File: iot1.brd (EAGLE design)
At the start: 95 x 100 mm, 77 parts, among them IC1 MEGA8-P, IC2 7805T, IC3 LTC2486C, IC4 7805T, IC5 4051N, IC6 OPA2134PA, IC8 MAX3468CPA, J1 DCJ0202, U2 HTU21D, U3 LM2577T-ADJ/NOPB, X1 22-23-2041, X2 A1944-50, X4 22-23-2041, X5 22-23-2041

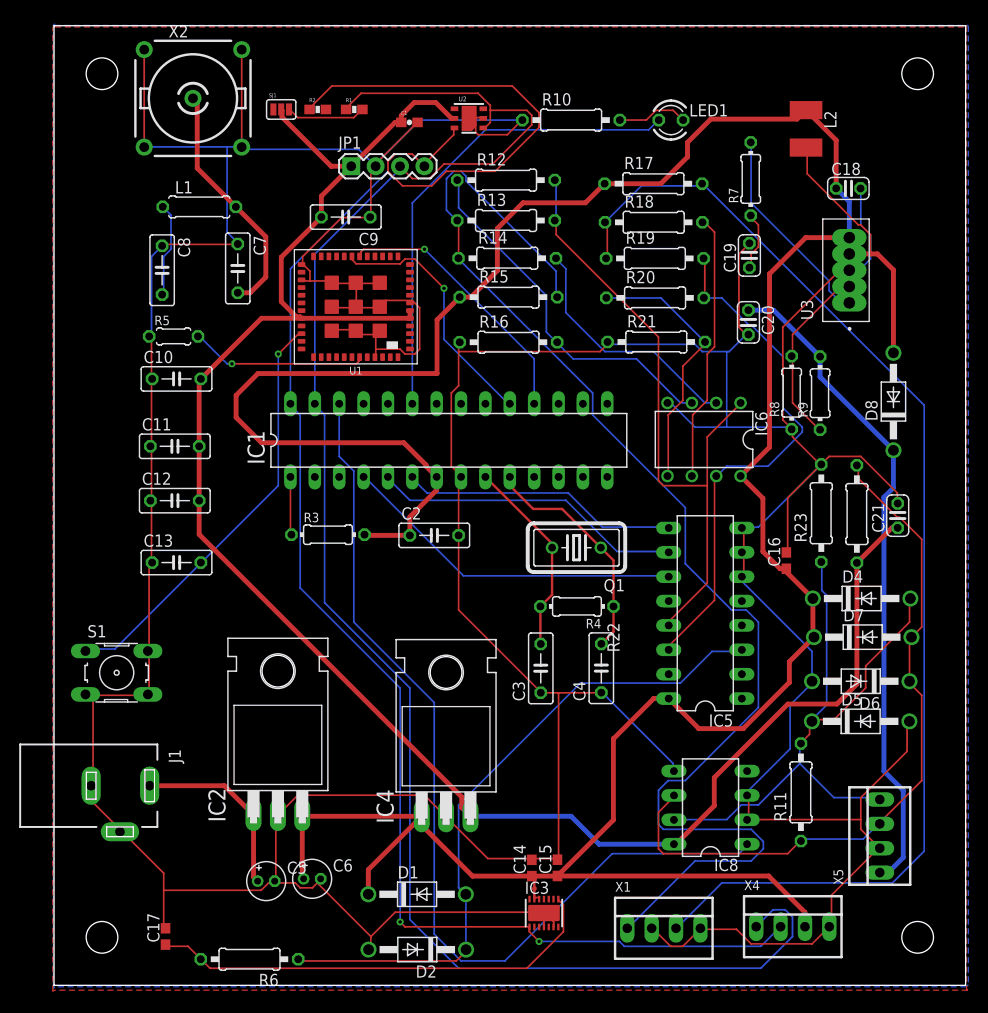
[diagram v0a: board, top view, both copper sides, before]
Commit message: renumbering board components
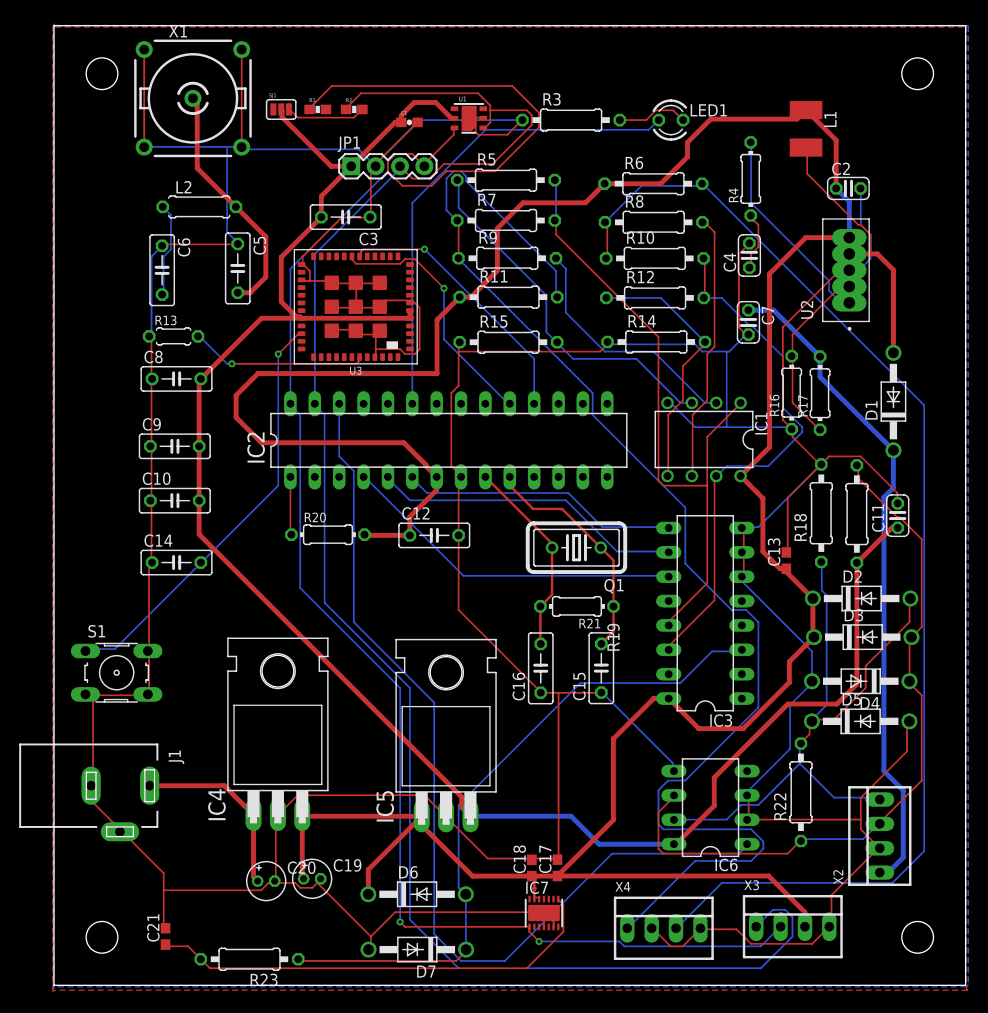
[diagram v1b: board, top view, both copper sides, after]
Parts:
- removed D8: 1N4004, diode:DO41-10
- removed IC8: MAX3468CPA, maxim:DIL08
- removed X5: 22-23-2041, con-molex:22-23-2041
- added D3: 1N4004, diode:DO41-10
- added IC7: LTC2486C, linear-technology:DFN14-4X3
- added X3: 22-23-2041, con-molex:22-23-2041
- C10: value 0.1u -> 10u
- C11: value 1u -> (none); device rcl:C050-025X075 -> rcl:C025-024X044
- C12: value 10u -> (none)
- C13: value 0.1u -> (none); device rcl:C050-025X075 -> rcl:C0603
- C14: value (none) -> 0.1u; device rcl:C0603 -> rcl:C050-025X075
- C15, C16: device rcl:C0603 -> rcl:C050-025X075
- C18: value 0.1uF -> (none); device rcl:C025-024X044 -> rcl:C0603
- C19: value 0.33uF -> (none); device rcl:C025-024X044 -> rcl:E1,8-4
- C2: value (none) -> 0.1uF; device rcl:C050-025X075 -> rcl:C025-024X044
- C20: value 680uF -> (none); device rcl:C025-024X044 -> rcl:E1,8-4
- C21: device rcl:C025-024X044 -> rcl:C0603
- C3: value (none) -> 1u
- C4: value (none) -> 0.33uF; device rcl:C050-025X075 -> rcl:C025-024X044
- C5, C6: device rcl:E1,8-4 -> rcl:C050-025X075
- C7: value (none) -> 680uF; device rcl:C050-025X075 -> rcl:C025-024X044
- C8: value (none) -> 0.1u
- IC1: value MEGA8-P -> OPA2134PA; device atmel:DIL28-3 -> linear:DIL08
- IC2: value 7805T -> MEGA8-P; device linear:TO220H -> atmel:DIL28-3
- IC3: value LTC2486C -> 4051N; device linear-technology:DFN14-4X3 -> 40xx:DIL16
- IC5: value 4051N -> 7805T; device 40xx:DIL16 -> linear:TO220H
- IC6: value OPA2134PA -> MAX3468CPA; device linear:DIL08 -> maxim:DIL08
- L1: value (none) -> 100uH; device rcl:0207/7 -> rcl:L1812
- L2: value 100uH -> (none); device rcl:L1812 -> rcl:0207/7
- R10: value 680 -> (none)
- R13: value (none) -> 10k; device rcl:0207/10 -> rcl:0204/5
- R16: value (none) -> 2k; device rcl:0207/10 -> rcl:0204/7
- R17: value (none) -> 17.4k; device rcl:0207/10 -> rcl:0204/7
- R20, R21: device rcl:0207/10 -> rcl:0204/7
- R3: value (none) -> 680; device rcl:0204/7 -> rcl:0207/10
- R4: value (none) -> 2.2k
- R5: value 10k -> (none); device rcl:0204/5 -> rcl:0207/10
- R7: value 2.2k -> (none); device rcl:0204/7 -> rcl:0207/10
- R8: value 2k -> (none); device rcl:0204/7 -> rcl:0207/10
- R9: value 17.4k -> (none); device rcl:0204/7 -> rcl:0207/10
- U1: value (none) -> HTU21D; device FaBo-LoRa:CMWX1ZZABZ -> SparkFun-Sensors:HTU21D
- U2: value HTU21D -> LM2577T-ADJ/NOPB; device SparkFun-Sensors:HTU21D -> LM2577T-ADJ_NOPB:VREG_LM2577T-ADJ/NOPB
- U3: value LM2577T-ADJ/NOPB -> (none); device LM2577T-ADJ_NOPB:VREG_LM2577T-ADJ/NOPB -> FaBo-LoRa:CMWX1ZZABZ
- X1: value 22-23-2041 -> A1944-50; device con-molex:22-23-2041 -> con-coax:A1944
- X2: value A1944-50 -> 22-23-2041; device con-coax:A1944 -> con-molex:22-23-2041
- moved STANDOFF2 123.8 mm to (90.0, 95.0)
- moved STANDOFF3 123.8 mm to (5.00, 5.00)
- moved X2 105.0 mm to (86.1, 15.6), turned to 90 degrees
- moved X1 99.4 mm to (14.5, 92.4)
- moved R6 91.1 mm to (62.5, 83.5), turned to 0 degrees
- moved C21 88.0 mm to (11.6, 5.09)
- moved C19 79.3 mm to (26.9, 11.1), turned to 0 degrees
- moved C18 78.1 mm to (49.8, 12.2), turned to 90 degrees
- moved C20 76.9 mm to (22.1, 10.9), turned to 0 degrees
- moved C11 75.7 mm to (87.9, 48.9), turned to 90 degrees
- moved R23 75.6 mm to (20.4, 2.72), turned to 180 degrees
- moved D1 71.4 mm to (87.5, 60.8), turned to 90 degrees
- moved C6 65.3 mm to (11.3, 74.5), turned to 270 degrees
- moved C5 63.9 mm to (19.2, 74.7), turned to 270 degrees
- moved L1 63.8 mm to (78.4, 89.3), turned to 270 degrees
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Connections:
- removed net N$50 (its old number): IC5.5
- new net N$31: IC7.5
- net 12V: now also C7.1, D1.C, R17.2, X2.1; no longer C20.1, D8.C, R9.2, X5.1
- net 3.3V: now also C11.1, C3.2, C8.2, IC5.3, IC6.8, R19.1, U1.VDD, U3.32, U3.5, U3.6; no longer C11.2, C12.2, C21.1, IC4.3, IC8.8, R22.1, U1.32, U1.5, U1.6, U2.VDD
- net 485A: now also D3.A, D4.C, IC6.6, R19.2, R22.1, X2.3; no longer D6.C, D7.A, IC8.6, R11.1, R22.2, X5.3
- net 485B: now also D2.A, IC6.7, R18.1, R22.2, X2.4; no longer D4.A, IC8.7, R11.2, R23.1, X5.4
- net 5V: now also C12.1, C13.1, C17.1, C19.+, D2.C, D3.C, D6.C, IC1.8, IC2.7, IC3.16, IC4.3, IC5.1, IC7.12, IC7.13, L1.1, R11.1, R20.2, R6.1, U2.5, X3.3; no longer C14.1, C15.1, C16.1, C6.+, D1.C, D4.C, D7.C, IC1.7, IC2.3, IC3.12, IC3.13, IC4.1, IC5.16, IC6.8, L2.1, R15.1, R17.1, R3.2, U3.5, X4.3
- net GND: now also C11.2, C12.2, C13.2, C14.1, C15.1, C16.1, C19.-, C20.-, C4.2, C5.1, C6.1, C7.2, D4.A, D7.A, IC1.4, IC2.8, IC3.7, IC3.8, IC5.2, IC6.2, IC6.3, IC6.5, IC7.14, IC7.4, IC7.6, IC7.EXP, R13.1, R14.1, R15.1, R18.2, R3.1, U1.GND, U2.3, U3.25, U3.27, U3.44, U3.49, U3.50, U3.51, U3.52, U3.53, U3.54, U3.55, U3.56, U3.57, U3.7, X1.3, X1.5, X3.4, X4.2; no longer C11.1, C12.1, C13.1, C14.2, C15.2, C16.2, C19.2, C20.2, C4.1, C5.-, C6.-, C7.1, D2.A, D6.A, IC1.8, IC2.2, IC3.14, IC3.4, IC3.EXP, IC5.6, IC5.7, IC5.8, IC6.4, IC8.2, IC8.3, IC8.5, R10.1, R21.1, R23.2, R5.1, R8.1, U1.25, U1.27, U1.44, U1.49, U1.50, U1.51, U1.52, U1.53, U1.54, U1.55, U1.56, U1.57, U2.7, U2.GND, U3.3, X2.3, X2.4, X2.5, X5.2
- net MUX_0: now also IC2.4, IC3.11; no longer IC1.4, IC5.11
- net MUX_1: now also IC2.5, IC3.10; no longer IC1.5, IC5.10
- net MUX_2: now also IC2.6, IC3.9; no longer IC1.6, IC5.9
- net N$1: now also U3.12; no longer U1.12
- net N$10: now also U3.3; no longer U1.3
- net N$11: now also U3.2; no longer U1.2
- net N$12: now also U3.1; no longer U1.1
- net N$13: now also R2.2; no longer R1.2
- net N$14: now also R1.2; no longer R2.2
- net N$15: now also IC2.23; no longer IC1.23
- net N$16: now also IC2.24; no longer IC1.24
- net N$17: now also U3.13; no longer U1.13
- net N$18: now also U3.14; no longer U1.14
- net N$19: now also U3.15; no longer U1.15
- net N$2: now also U3.11; no longer U1.11
- net N$20: now also U3.16; no longer U1.16
- net N$21: now also U3.17; no longer U1.17
- net N$22: now also IC2.25; no longer IC1.25
- net N$24: now also U3.20; no longer U1.20
- net N$25: now also U3.21; no longer U1.21
- net N$26: now also U3.22; no longer U1.22
- net N$27: now also U3.23; no longer U1.23
- net N$28: now also U3.24; no longer U1.24
- net N$29: now also IC3.12; no longer IC5.12
- net N$3: now also U3.10; no longer U1.10
- net N$30: now also C6.2, L2.1, U3.26; no longer C8.2, L1.1, U1.26
- net N$32: now also U3.28; no longer U1.28
- net N$33: now also U3.29; no longer U1.29
- net N$34: now also U3.30; no longer U1.30
- net N$35: now also U3.31; no longer U1.31
- net N$36: now also IC3.1; no longer IC5.1
- net N$37: now also U3.33; no longer U1.33
- net N$38: now also C14.2, U3.34; no longer C13.2, U1.34
- net N$39: now also U3.35; no longer U1.35
- net N$4: now also U3.9; no longer U1.9
- net N$40: now also U3.36; no longer U1.36
- net N$41: now also IC2.2; no longer IC1.2
- net N$42: now also IC2.3; no longer IC1.3
- net N$45: now also D1.A, L1.2, U2.4; no longer D8.A, L2.2, U3.4
- net N$46: now also U3.48; no longer U1.48
- net N$47: now also U3.47; no longer U1.47
- net N$48: now also U3.46; no longer U1.46
- net N$49: now also U3.45; no longer U1.45
- net N$5: now also U3.8; no longer U1.8
- net N$51: now also R13.2, U3.43; no longer R5.2, U1.43
- net N$52: now also U3.42; no longer U1.42
- net N$53: now also U3.41; no longer U1.41
- net N$54: now also U3.40; no longer U1.40
- net N$55: now also U3.39; no longer U1.39
- net N$56: now also U3.38; no longer U1.38
- net N$57: now also U3.37; no longer U1.37
- net N$58: now also IC2.11; no longer IC1.11
- net N$59: now also IC2.12; no longer IC1.12
- net N$6: now also U3.4; no longer U1.4
- net N$60: now also IC2.13; no longer IC1.13
- net N$61: now also IC2.14; no longer IC1.14
- net N$62: now also IC2.15; no longer IC1.15
- net N$63: now also IC2.16; no longer IC1.16
- net N$64: now also IC2.17; no longer IC1.17
- net N$65: now also IC3.2; no longer IC5.2
- net N$66: now also IC3.4; no longer IC5.4
- net N$67: now also IC2.1, R20.1; no longer IC1.1, R3.1
- net N$68: now also IC2.22; no longer IC1.22
- net N$69: now also IC2.21; no longer IC1.21
- net N$70: now also IC2.20; no longer IC1.20
- net N$71: now also IC7.11; no longer IC3.11
- net N$72: now also C15.2, IC2.10, R21.1; no longer C4.2, IC1.10, R4.1
- net N$73: now also C16.2, IC2.9, R21.2; no longer C3.2, IC1.9, R4.2
- net N$74: now also IC7.10; no longer IC3.10
- net N$75: now also IC7.9; no longer IC3.9
- net N$76: now also R3.2; no longer R10.2
- net N$77: now also IC7.7; no longer IC3.7
- net N$78: now also IC1.3, R15.2, R5.1; no longer IC6.3, R12.1, R16.2
- net N$81: now also IC1.2, R9.2; no longer IC6.2, R14.2
- net N$82: now also IC1.5, R12.1, R14.2; no longer IC6.5, R20.1, R21.2
- net N$83: now also IC1.6, R8.2; no longer IC6.6, R18.2
- net N$84: now also R4.2, U2.1; no longer R7.2, U3.1
- net N$85: now also C4.1, R4.1; no longer C19.1, R7.1
- net N$87: now also R16.2, R17.1, U2.2; no longer R8.2, R9.1, U3.2
- net N$88: now also IC6.4; no longer IC8.4
- net N$9: now also IC3.15; no longer IC5.15
- net RF_LORAWAN: now also C5.2, L2.2, X1.1; no longer C7.2, L1.2, X2.1
- net RX: now also IC2.18, U3.18; no longer IC1.18, U1.18
- net S: now also D6.A, D7.C, IC3.3, R23.1; no longer D1.A, D2.C, IC5.3, R6.1
- net SCL: now also IC2.28, IC7.1, IC7.3, R1.1, U1.SCK, X3.2; no longer IC1.28, IC3.1, IC3.3, R2.1, U2.SCK, X4.2
- net SDA: now also IC2.27, IC7.2, R2.1, U1.DATA, X3.1; no longer IC1.27, IC3.2, R1.1, U2.DATA, X4.1
- net SENSORS: now also C21.1, IC7.8, R23.2; no longer C17.1, IC3.8, R6.2
- net SOIL_MOISTURE_0: now also R11.2, R7.1, R9.1, X4.1; no longer R13.1, R14.1, R15.2, X1.1
- net SOIL_MOISTURE_1: now also R10.1, R6.2, R8.1, X4.3; no longer R17.2, R18.1, R19.1, X1.3
- net SOIL_MOISTURE_AMPLIFIED_0: now also IC1.1, IC3.13, R5.2, R7.2; no longer IC5.13, IC6.1, R12.2, R13.2
- net SOIL_MOISTURE_AMPLIFIED_1: now also IC1.7, IC3.14, R10.2, R12.2; no longer IC5.14, IC6.7, R19.2, R20.2
- net TX: now also IC2.19, U3.19; no longer IC1.19, U1.19
- net TX_485: now also IC2.26, IC6.1; no longer IC1.26, IC8.1
- net V_IN: now also C20.+, IC4.1; no longer C5.+, IC2.1

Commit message: adding component's values
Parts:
- C11, C19: value (none) -> 0.1uF
- C12, C13, C15, C16: value (none) -> 100nF
- C17: value (none) -> 0.1pF
- C18: value (none) -> 10pF
- C20: value (none) -> 0.22uF
- C21: value (none) -> 1uF
- Q1: value (none) -> 16MHz
- R10, R11, R12, R14, R15, R5, R6, R7, R8, R9: value (none) -> 220
- R18, R19: value (none) -> 360
- R20: value (none) -> 10k
- R21, R23: value (none) -> 1M
- R22: value (none) -> 120
